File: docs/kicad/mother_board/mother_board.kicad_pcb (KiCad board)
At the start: 2 copper layers, 148 x 93 mm, 37 parts, among them J1 ROW_BOARDS, J10 PEDAL1, J11 PEDAL2, J12 PEDAL3, J13 PEDAL4, J14 GUITAR_IN, J15 LINE_OUT, J16 LEDS, J2 ROTARIES, J3 TE_DISPLAY, J4 RPI_DISPLAY, J5 rPi_5V, J6 RPI_RUN, J7 rpi_connector, J8 I2S_TXB, J9 EigthInchJack1, Q1 BC547, U1 teensyAudioRevD_WithAudio, U2 myTeensy4.1

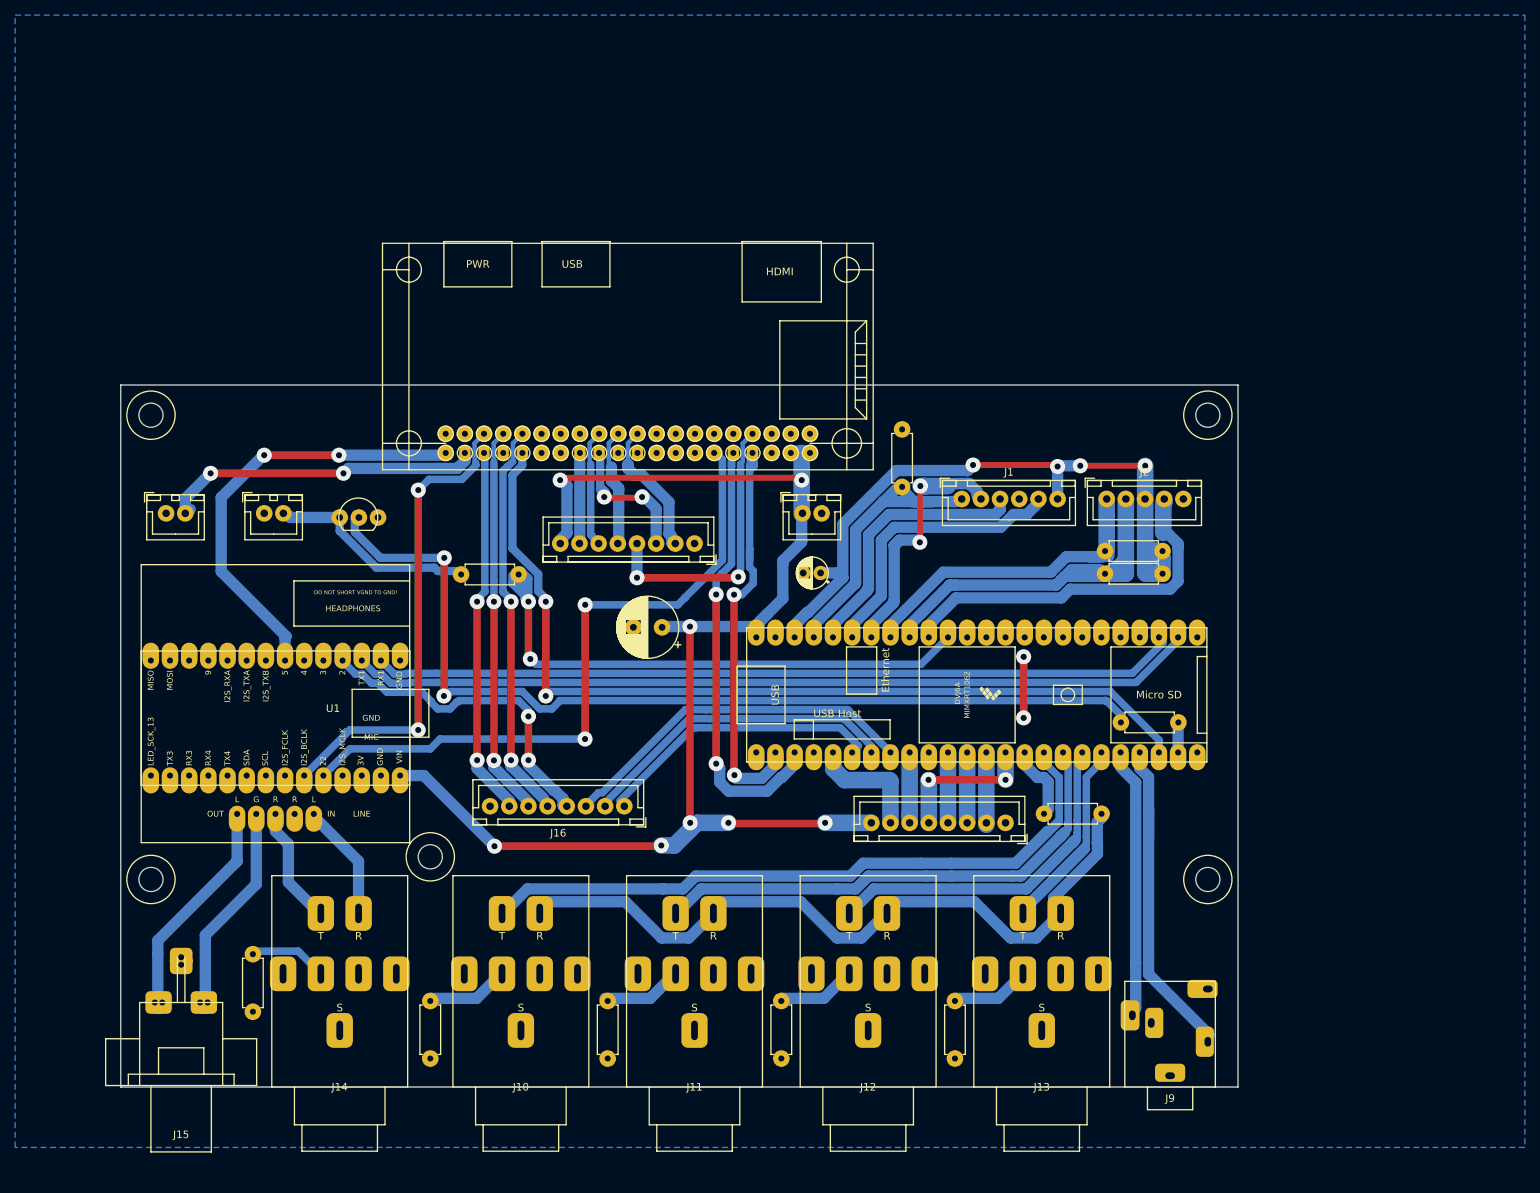
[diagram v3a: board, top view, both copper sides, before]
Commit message: PCB milling marathon - made 5 row_boards, rotary_board, led_board, and reworked detailed design of motherboard - motherboard *should* match old one that was milled and installed in initial TE3 box
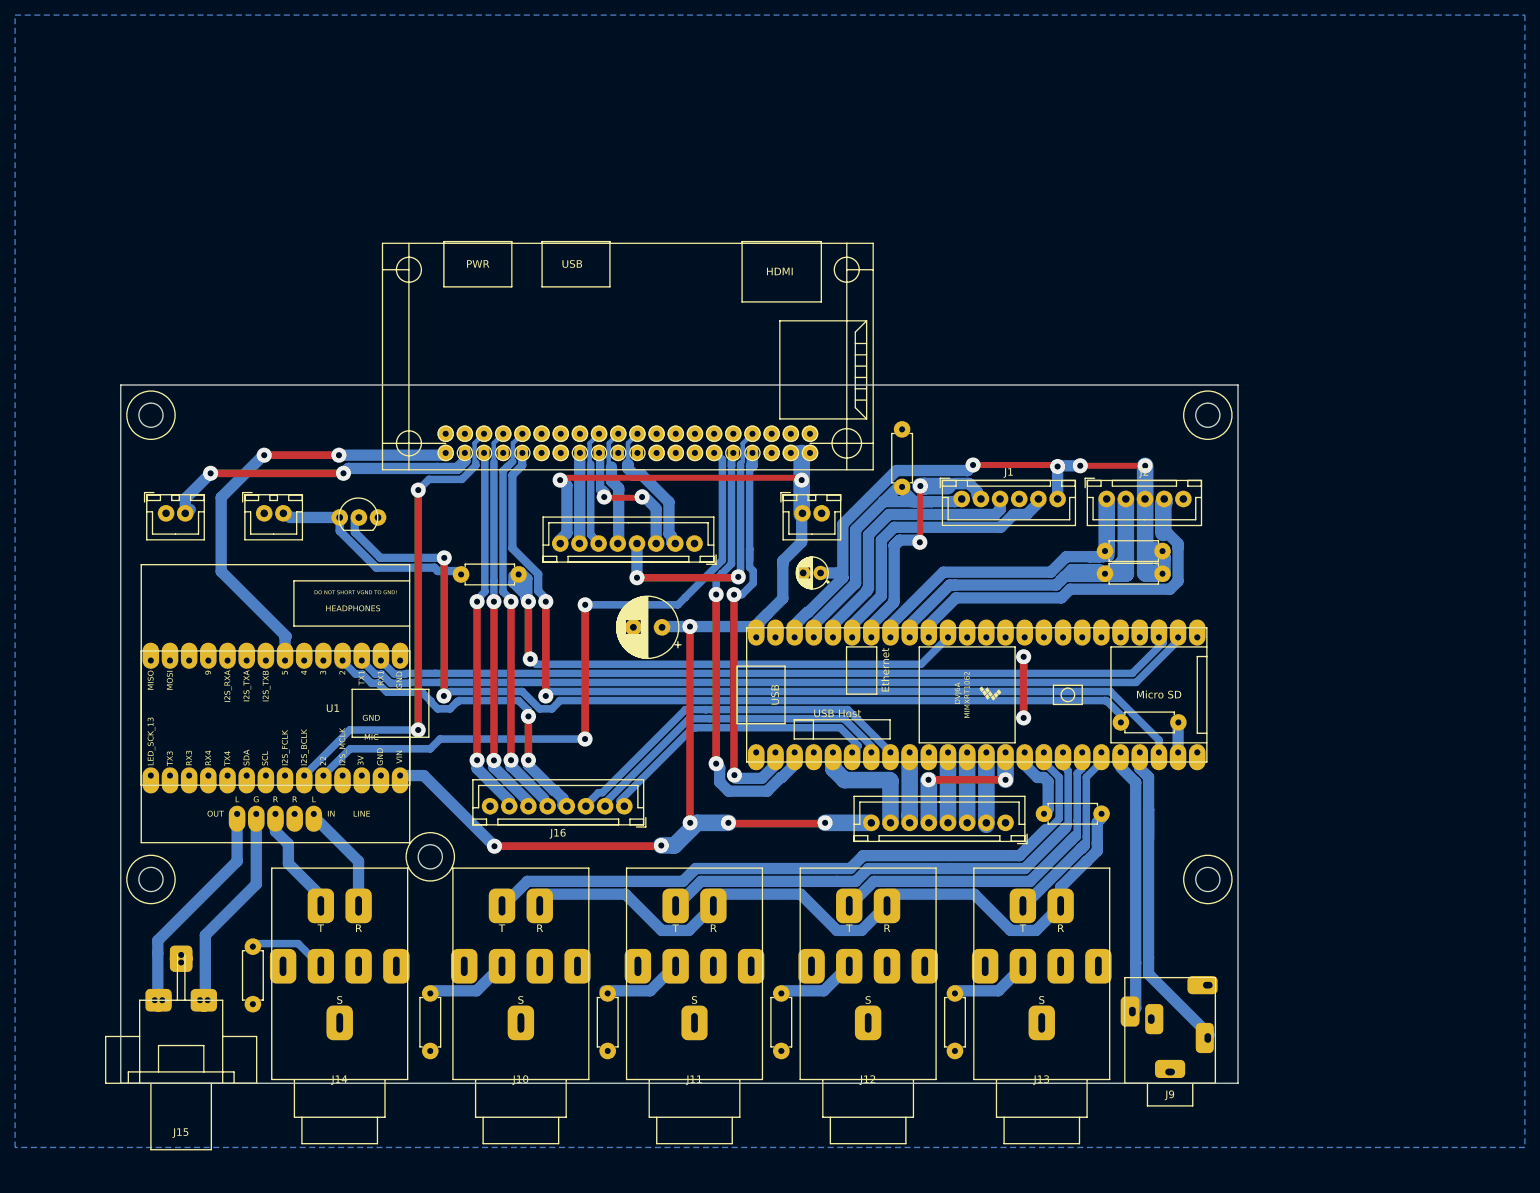
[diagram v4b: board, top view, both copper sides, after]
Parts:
- moved J10 1.00 mm to (117.0, 143.5)
- moved J11 1.00 mm to (140.0, 143.5)
- moved J12 1.00 mm to (163.0, 143.5)
- moved J13 1.00 mm to (186.0, 143.5)
- moved J14 1.00 mm to (93.0, 143.5)
- moved R10 1.00 mm to (81.5, 133.4)
- moved R6 1.00 mm to (105.0, 139.6)
- moved R7 1.00 mm to (128.5, 139.6)
- moved R8 1.00 mm to (151.5, 139.6)
- moved R9 1.00 mm to (174.5, 139.6)
- moved J9 0.50 mm to (203.0, 151.5)
- moved J15 0.30 mm to (72.0, 151.0)
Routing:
- net PEDAL4: track 28.7 -> 22.6 mm
- net PEDAL1: track 90.0 -> 87.0 mm
- net Net-(J10-PadR): track 95.5 -> 93.9 mm
- net PEDAL2: track 65.8 -> 66.8 mm
- net LINE_IN_L: track 15.1 -> 14.1 mm
- net LINE_IN_R: track 15.5 -> 14.7 mm
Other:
- board size 148 x 93 mm -> 148 x 92.5 mm

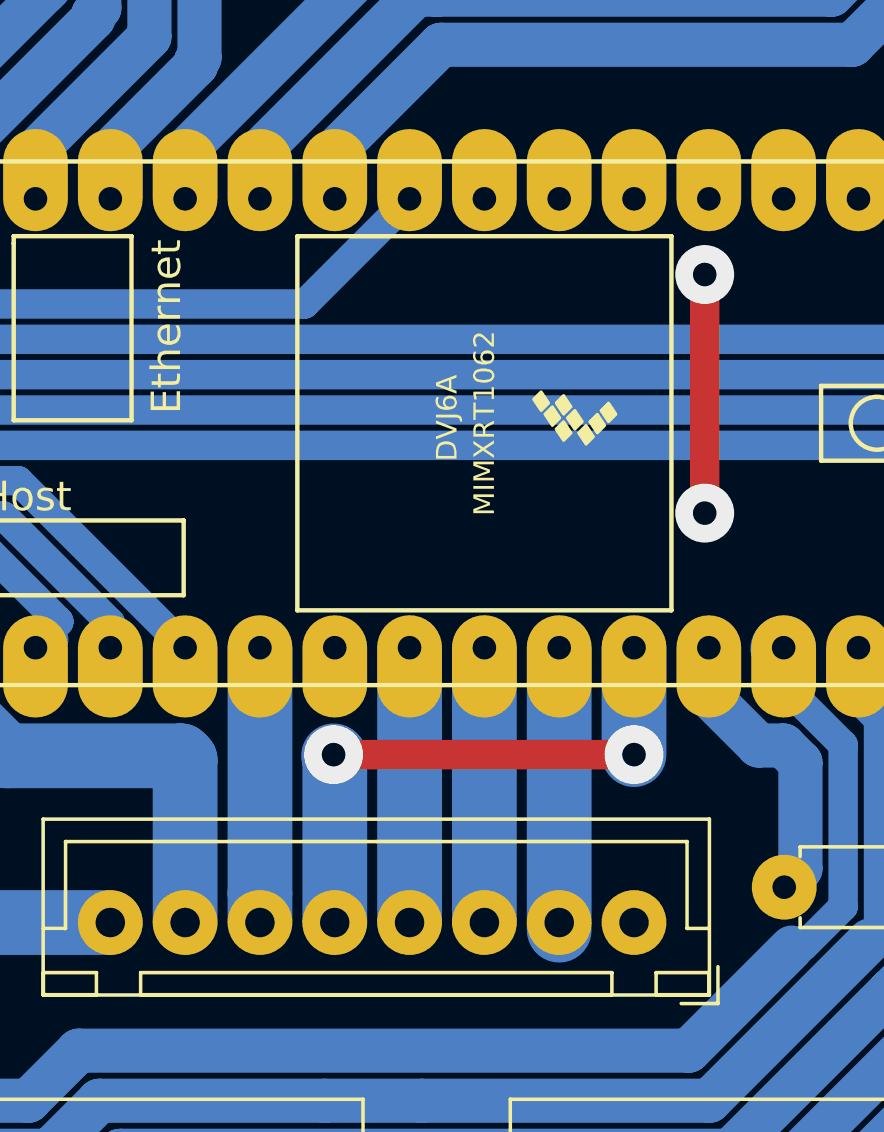
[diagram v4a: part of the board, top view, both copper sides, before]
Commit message: final initial TE3 PCBS - updated LED board green resistor to 1K - changed TE3 display SCLK to pin13 as it is required for hardware SPI0 - changed nomenclature of rotary board to ROT0..ROT4 and corrected order to match named rotary 1..4
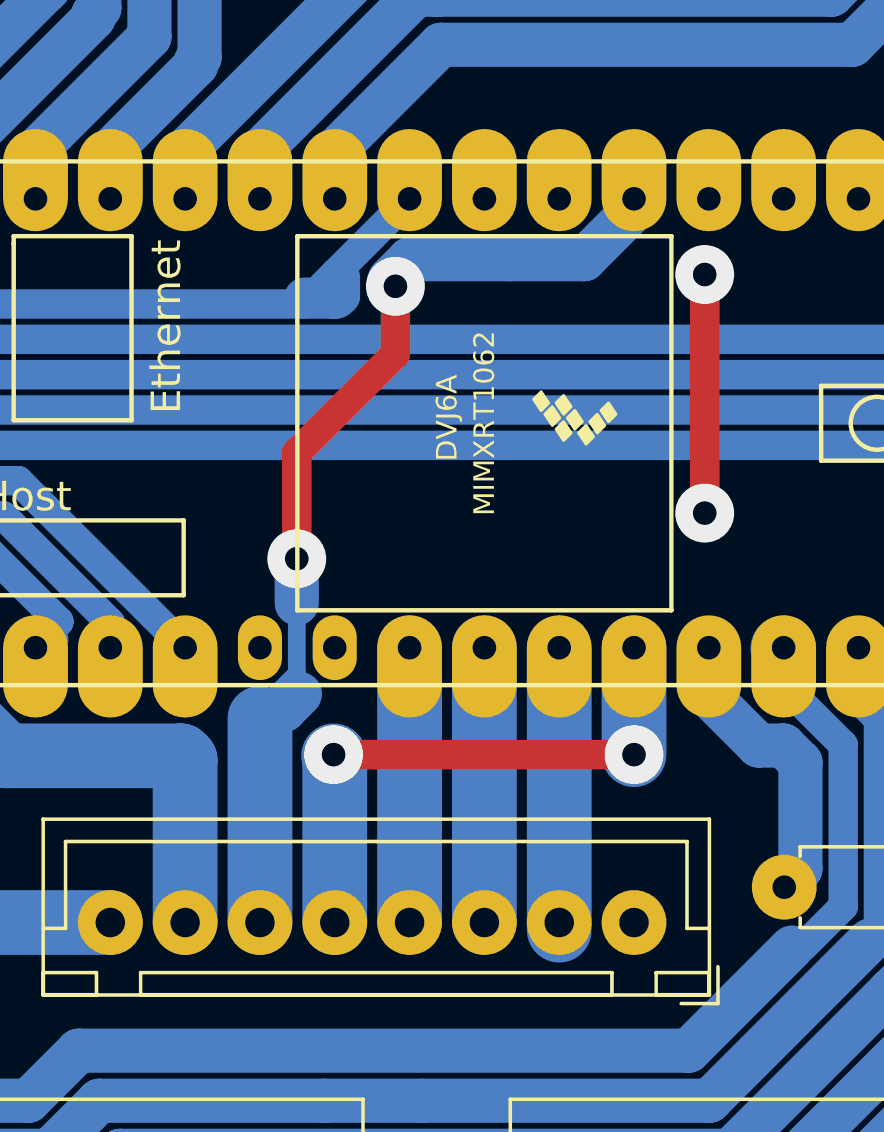
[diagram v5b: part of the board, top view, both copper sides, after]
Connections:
- U2 pad 35: Net-(U2-Pad35) -> T41_SCLK
- U2 pad 9: T41_SCLK -> Net-(U2-Pad9)
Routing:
- net T41_SCLK: track 9.23 -> 36.0 mm, vias 0 -> 2
- net SENS_PI_RUN: track 76.2 -> 77.4 mm

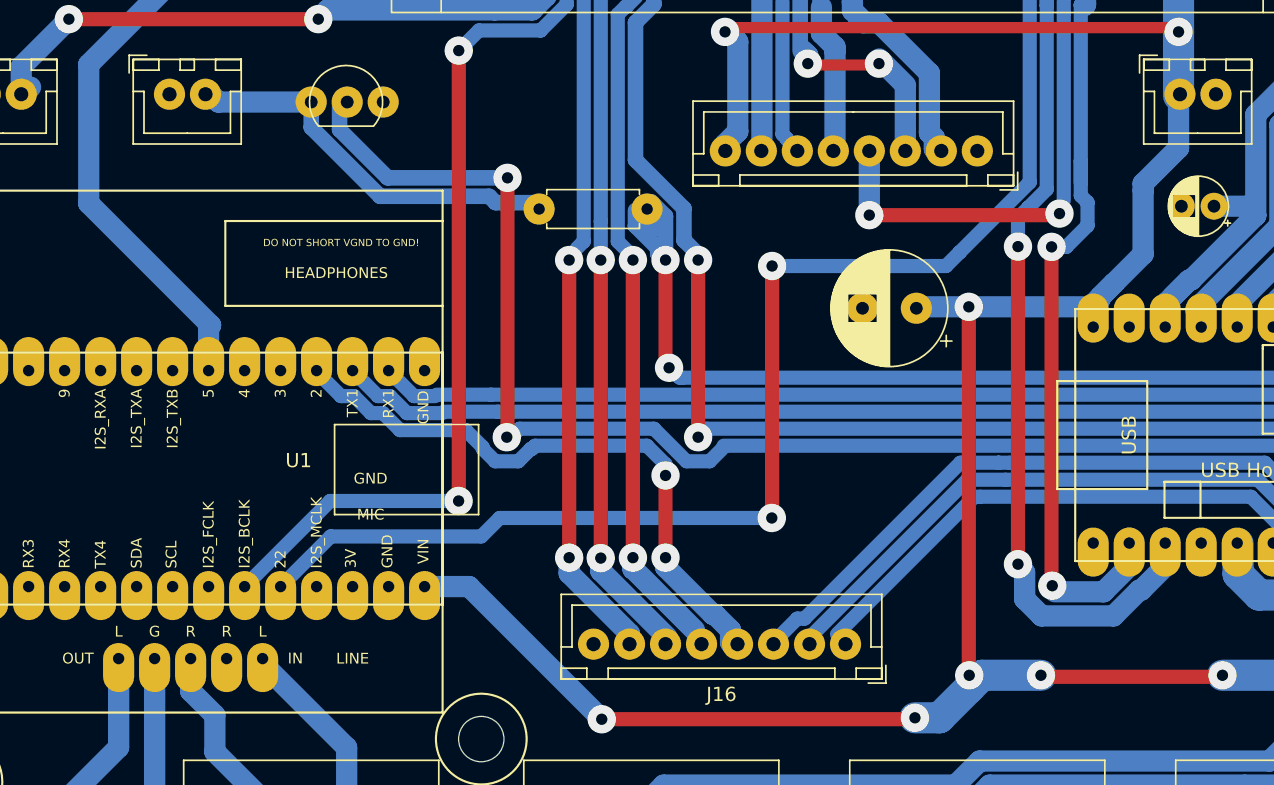
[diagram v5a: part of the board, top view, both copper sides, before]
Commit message: Fixed problems discovered after milling 1st test mother_board. - effing had I2S BCLK and FCLK going to wrong pins on teensy4.0!! - connector for revD audio pins was off by 1.5mm - separated rPI and teensy 5V rails - needed to use SCLK=pin13 on teensy4.1 for display deleted the old plot files
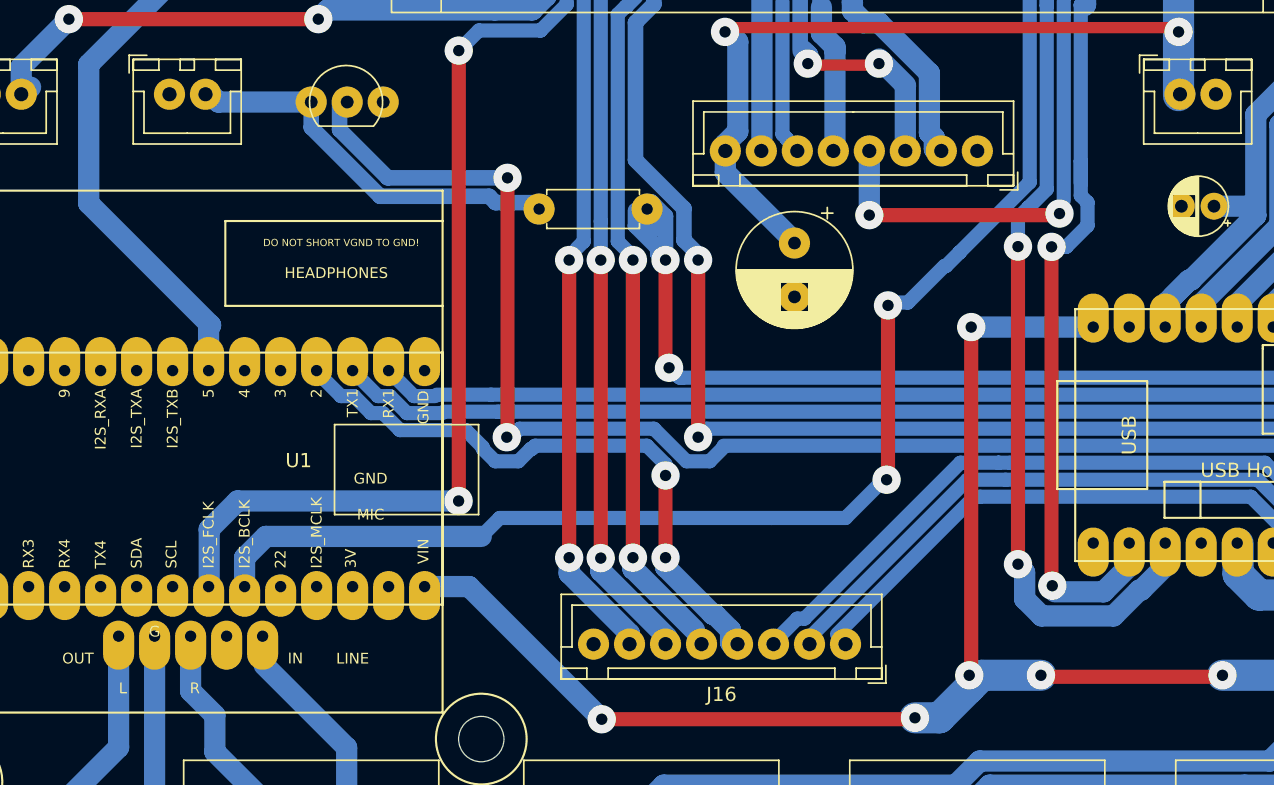
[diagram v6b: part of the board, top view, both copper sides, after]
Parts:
- moved C1 9.75 mm to (127.1, 86.5), turned to 270 degrees
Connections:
- C1 pad 1: +5V -> RPI_5V
- J4 pad 8: +5V -> RPI_5V
- J5 pad 1: +5V -> RPI_5V
- J7 pad 2: +5V -> RPI_5V
- J7 pad 4: +5V -> RPI_5V
- U1 pad 22: Net-(U1-Pad22) -> I2S_FCLK
- U1 pad 23: I2S_FCLK -> I2S_BCLK
- U1 pad 24: I2S_BCLK -> Net-(U1-Pad24)
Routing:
- net +5V: track 178.7 -> 102.7 mm, vias 8 -> 6
- net RPI_5V: track 0.00 -> 61.0 mm, vias 0 -> 2
- net I2S_FCLK: track 63.1 -> 68.0 mm
- net I2S_BCLK: track 90.0 -> 90.5 mm

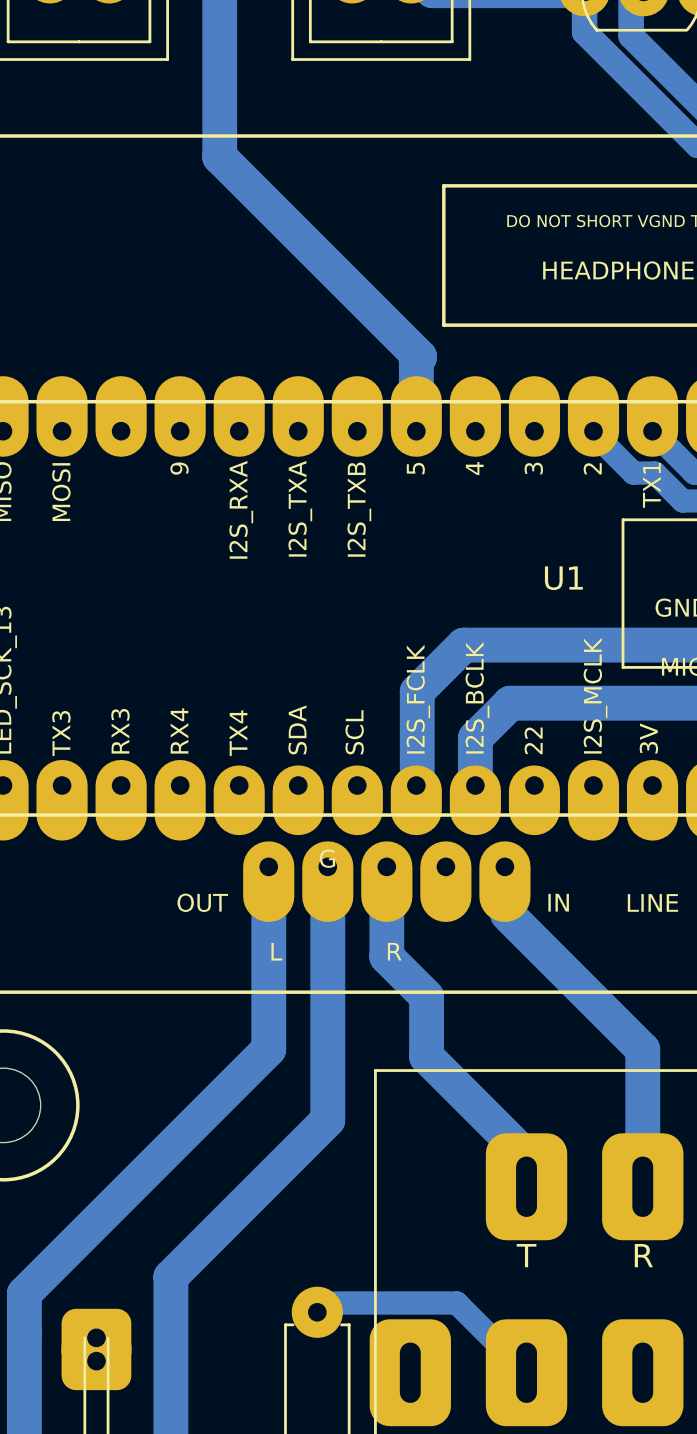
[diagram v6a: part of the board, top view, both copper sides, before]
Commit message: found, documented, and fixed test PCB problems with I2S_IXR, LINE_IN_R, GND, and LINE_OUT_R traces (bad schematic and bad kicad symbols)
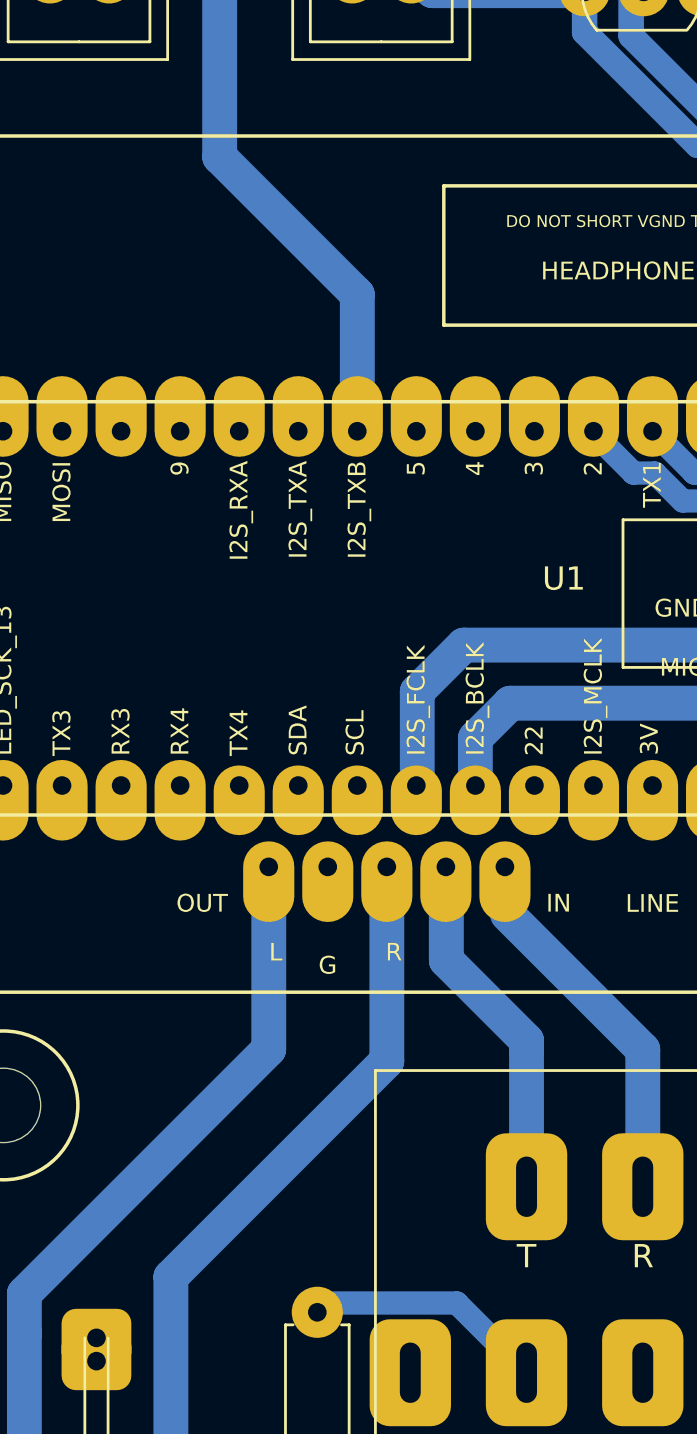
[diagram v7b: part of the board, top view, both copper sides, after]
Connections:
- U1 pad 30: GND -> LINE_IN_R
- U1 pad 31: LINE_IN_R -> LINE_OUT_R
- U1 pad 32: LINE_OUT_R -> GND
- U1 pad 7: I2S_RXB -> Net-(U1-Pad7)
- U1 pad 8: Net-(U1-Pad8) -> I2S_RXB
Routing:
- net LINE_OUT_R: track 27.5 -> 30.1 mm
- net I2S_RXB: track 57.4 -> 56.2 mm
- net LINE_IN_R: track 14.7 -> 15.7 mm
